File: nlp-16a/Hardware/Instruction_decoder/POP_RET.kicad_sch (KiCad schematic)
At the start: 12 parts

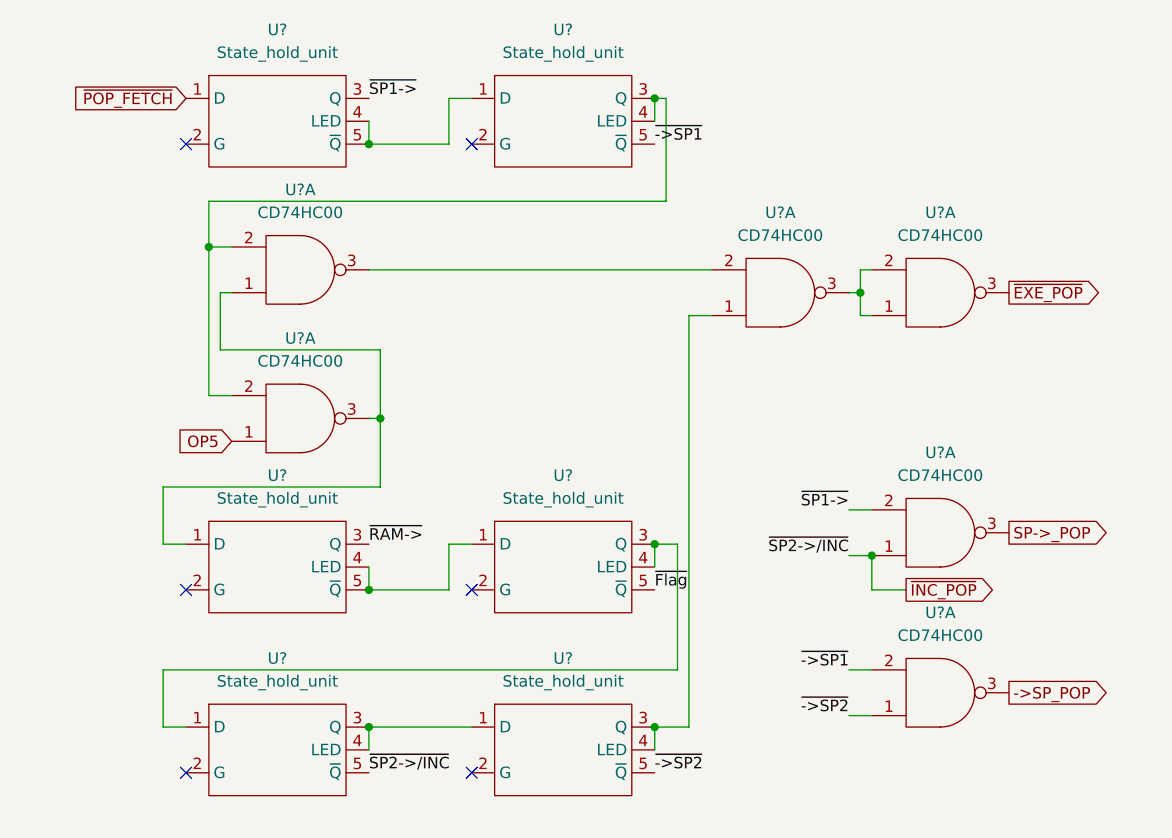
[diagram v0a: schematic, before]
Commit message: 命令デコーダ 不具合修正
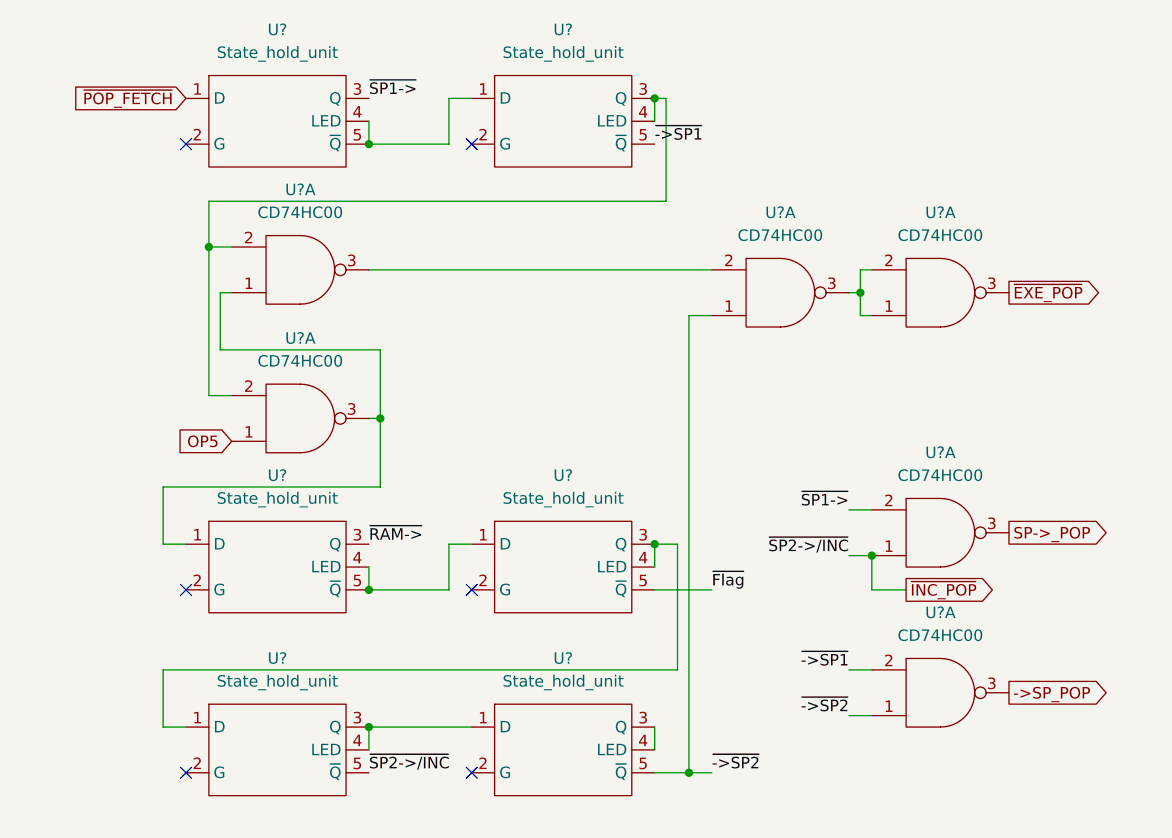
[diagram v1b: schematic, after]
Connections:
- net ~{->SP2}: now also U?.1
- net at U?.3 (Q), U?.4 (LED): no longer U?.1
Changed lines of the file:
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@@
   (junction (at 110.49 101.6) (diameter 0) (color 0 0 0 0)
   )
-  (junction (at 142.24 101.6) (diameter 0) (color 0 0 0 0)
-  )
   (junction (at 165.1 53.34) (diameter 0) (color 0 0 0 0)
   )
@@
   )
   (junction (at 142.24 81.28) (diameter 0) (color 0 0 0 0)
+  )
+  (junction (at 146.05 106.68) (diameter 0) (color 0 0 0 0)
   )
   (junction (at 110.49 36.83) (diameter 0) (color 0 0 0 0)
@@
     (stroke (width 0) (type default) (color 0 0 0 0))
   )
+  (wire (pts (xy 148.59 86.36) (xy 142.24 86.36))
+    (stroke (width 0) (type default) (color 0 0 0 0))
+  )
   (wire (pts (xy 111.76 67.31) (xy 111.76 74.93))
     (stroke (width 0) (type default) (color 0 0 0 0))
@@
     (stroke (width 0) (type default) (color 0 0 0 0))
   )
+  (wire (pts (xy 146.05 106.68) (xy 142.24 106.68))
+    (stroke (width 0) (type default) (color 0 0 0 0))
+  )
   (wire (pts (xy 142.24 31.75) (xy 143.51 31.75))
     (stroke (width 0) (type default) (color 0 0 0 0))
@@
     (stroke (width 0) (type default) (color 0 0 0 0))
   )
-  (wire (pts (xy 142.24 101.6) (xy 146.05 101.6))
-    (stroke (width 0) (type default) (color 0 0 0 0))
-  )
   (wire (pts (xy 142.24 31.75) (xy 142.24 34.29))
     (stroke (width 0) (type default) (color 0 0 0 0))
@@
     (stroke (width 0) (type default) (color 0 0 0 0))
   )
-  (wire (pts (xy 146.05 101.6) (xy 146.05 55.88))
+  (wire (pts (xy 146.05 55.88) (xy 146.05 106.68))
     (stroke (width 0) (type default) (color 0 0 0 0))
   )
@@
     (stroke (width 0) (type default) (color 0 0 0 0))
   )
+  (wire (pts (xy 148.59 106.68) (xy 146.05 106.68))
+    (stroke (width 0) (type default) (color 0 0 0 0))
+  )
   (wire (pts (xy 144.78 81.28) (xy 144.78 95.25))
     (stroke (width 0) (type default) (color 0 0 0 0))
@@
     (effects (font (size 1.27 1.27)) (justify left bottom))
   )
-  (label "~{Flag}" (at 142.24 86.36 0)
-    (effects (font (size 1.27 1.27)) (justify left bottom))
-  )
-  (label "~{->SP2}" (at 142.24 106.68 0)
-    (effects (font (size 1.27 1.27)) (justify left bottom))
-  )
+  (label "~{Flag}" (at 148.59 86.36 0)
+    (effects (font (size 1.27 1.27)) (justify left bottom))
+  )
+  (label "~{->SP2}" (at 148.59 106.68 0)
+    (effects (font (size 1.27 1.27)) (justify left bottom))
+  )

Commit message: 命令デコーダ ロジック部の設計だいたい完了git statusgit statusやったぜ
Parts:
- removed U? (x2): CD74HC00, Package_DIP:DIP-14_W7.62mm, symbol CD74HCXX:CD74HC00
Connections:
- net ~{->SP1} renamed ~{->SP_SET}
- net ~{->SP2} renamed ~{->SP_INC_RET}
- net ~{Flag} renamed ~{->Flag_Return}
- net ~{INC_POP} renamed ~{SP_INC_RET->}
- net ~{RAM->} renamed ~{Flag_Return->}
- net ~{SP1->} renamed ~{SP_SET->}
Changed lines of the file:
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@@
   (junction (at 165.1 53.34) (diameter 0) (color 0 0 0 0)
-  )
-  (junction (at 166.37 82.55) (diameter 0) (color 0 0 0 0)
   )
   (junction (at 142.24 31.75) (diameter 0) (color 0 0 0 0)
@@
   (no_connect (at 121.92 86.36))
   (no_connect (at 90.17 106.68))
-  (wire (pts (xy 166.37 82.55) (xy 166.37 86.36))
+  (wire (pts (xy 142.24 36.83) (xy 148.59 36.83))
     (stroke (width 0) (type default) (color 0 0 0 0))
   )
@@
     (stroke (width 0) (type default) (color 0 0 0 0))
   )
+  (wire (pts (xy 113.03 73.66) (xy 148.59 73.66))
+    (stroke (width 0) (type default) (color 0 0 0 0))
+  )
   (wire (pts (xy 146.05 55.88) (xy 148.59 55.88))
     (stroke (width 0) (type default) (color 0 0 0 0))
@@
     (stroke (width 0) (type default) (color 0 0 0 0))
   )
+  (wire (pts (xy 111.76 31.75) (xy 111.76 26.67))
+    (stroke (width 0) (type default) (color 0 0 0 0))
+  )
   (wire (pts (xy 142.24 81.28) (xy 144.78 81.28))
     (stroke (width 0) (type default) (color 0 0 0 0))
@@
     (stroke (width 0) (type default) (color 0 0 0 0))
   )
+  (wire (pts (xy 110.49 31.75) (xy 111.76 31.75))
+    (stroke (width 0) (type default) (color 0 0 0 0))
+  )
   (wire (pts (xy 143.51 43.18) (xy 92.71 43.18))
     (stroke (width 0) (type default) (color 0 0 0 0))
@@
     (stroke (width 0) (type default) (color 0 0 0 0))
   )
+  (wire (pts (xy 111.76 106.68) (xy 111.76 110.49))
+    (stroke (width 0) (type default) (color 0 0 0 0))
+  )
   (wire (pts (xy 142.24 101.6) (xy 142.24 104.14))
     (stroke (width 0) (type default) (color 0 0 0 0))
@@
     (stroke (width 0) (type default) (color 0 0 0 0))
   )
-  (wire (pts (xy 163.83 82.55) (xy 166.37 82.55))
-    (stroke (width 0) (type default) (color 0 0 0 0))
-  )
-  (wire (pts (xy 170.18 86.36) (xy 166.37 86.36))
+  (wire (pts (xy 113.03 81.28) (xy 113.03 73.66))
+    (stroke (width 0) (type default) (color 0 0 0 0))
+  )
+  (wire (pts (xy 111.76 110.49) (xy 148.59 110.49))
     (stroke (width 0) (type default) (color 0 0 0 0))
   )
@@
     (stroke (width 0) (type default) (color 0 0 0 0))
   )
-  (wire (pts (xy 163.83 77.47) (xy 166.37 77.47))
+  (wire (pts (xy 110.49 106.68) (xy 111.76 106.68))
+    (stroke (width 0) (type default) (color 0 0 0 0))
+  )
+  (wire (pts (xy 110.49 81.28) (xy 113.03 81.28))
     (stroke (width 0) (type default) (color 0 0 0 0))
   )
@@
     (stroke (width 0) (type default) (color 0 0 0 0))
   )
+  (wire (pts (xy 111.76 26.67) (xy 148.59 26.67))
+    (stroke (width 0) (type default) (color 0 0 0 0))
+  )
   (wire (pts (xy 90.17 101.6) (xy 87.63 101.6))
     (stroke (width 0) (type default) (color 0 0 0 0))
@@
     (stroke (width 0) (type default) (color 0 0 0 0))
   )
-  (wire (pts (xy 163.83 95.25) (xy 166.37 95.25))
-    (stroke (width 0) (type default) (color 0 0 0 0))
-  )
   (wire (pts (xy 143.51 31.75) (xy 143.51 43.18))
     (stroke (width 0) (type default) (color 0 0 0 0))
@@
     (stroke (width 0) (type default) (color 0 0 0 0))
   )
-  (wire (pts (xy 163.83 100.33) (xy 166.37 100.33))
-    (stroke (width 0) (type default) (color 0 0 0 0))
-  )
   (wire (pts (xy 163.83 53.34) (xy 165.1 53.34))
     (stroke (width 0) (type default) (color 0 0 0 0))
@@
     (stroke (width 0) (type default) (color 0 0 0 0))
   )
-  (label "~{SP1->}" (at 163.83 77.47 180)
-    (effects (font (size 1.27 1.27)) (justify right bottom))
-  )
-  (label "~{->SP1}" (at 163.83 95.25 180)
-    (effects (font (size 1.27 1.27)) (justify right bottom))
-  )
-  (label "~{SP2->{slash}INC}" (at 110.49 106.68 0)
-    (effects (font (size 1.27 1.27)) (justify left bottom))
-  )
-  (label "~{->SP2}" (at 163.83 100.33 180)
-    (effects (font (size 1.27 1.27)) (justify right bottom))
-  )
-  (label "~{SP2->{slash}INC}" (at 163.83 82.55 180)
-    (effects (font (size 1.27 1.27)) (justify right bottom))
-  )
-  (label "~{SP1->}" (at 110.49 31.75 0)
-    (effects (font (size 1.27 1.27)) (justify left bottom))
-  )
-  (label "~{RAM->}" (at 110.49 81.28 0)
-    (effects (font (size 1.27 1.27)) (justify left bottom))
-  )
-  (label "~{->SP1}" (at 142.24 36.83 0)
-    (effects (font (size 1.27 1.27)) (justify left bottom))
-  )
-  (label "~{Flag}" (at 148.59 86.36 0)
-    (effects (font (size 1.27 1.27)) (justify left bottom))
-  )
-  (label "~{->SP2}" (at 148.59 106.68 0)
-    (effects (font (size 1.27 1.27)) (justify left bottom))
-  )
   (global_label "~{EXE_POP}" (shape output) (at 181.61 53.34 0) (fields_autoplaced)
     (effects (font (size 1.27 1.27)) (justify left))
     (property "Intersheet References" "${INTERSHEET_REFS}" (id 0) (at 192.3688 53.2606 0)
+      (effects (font (size 1.27 1.27)) (justify left) hide)
+    )
+  )
+  (global_label "~{SP_INC_RET->}" (shape output) (at 148.59 110.49 0) (fields_autoplaced)
+    (effects (font (size 1.27 1.27)) (justify left))
+    (property "Intersheet References" "${INTERSHEET_REFS}" (id 0) (at 165.1545 110.4106 0)
       (effects (font (size 1.27 1.27)) (justify left) hide)
     )
@@
     )
   )
-  (global_label "SP->_POP" (shape output) (at 181.61 80.01 0) (fields_autoplaced)
-    (effects (font (size 1.27 1.27)) (justify left))
-    (property "Intersheet References" "${INTERSHEET_REFS}" (id 0) (at 194.4855 79.9306 0)
+  (global_label "~{->SP_INC_RET}" (shape output) (at 148.59 106.68 0) (fields_autoplaced)
+    (effects (font (size 1.27 1.27)) (justify left))
+    (property "Intersheet References" "${INTERSHEET_REFS}" (id 0) (at 165.1545 106.6006 0)
+      (effects (font (size 1.27 1.27)) (justify left) hide)
+    )
+  )
+  (global_label "~{SP_SET->}" (shape output) (at 148.59 26.67 0) (fields_autoplaced)
+    (effects (font (size 1.27 1.27)) (justify left))
+    (property "Intersheet References" "${INTERSHEET_REFS}" (id 0) (at 160.9212 26.5906 0)
+      (effects (font (size 1.27 1.27)) (justify left) hide)
+    )
+  )
+  (global_label "~{->SP_SET}" (shape output) (at 148.59 36.83 0) (fields_autoplaced)
+    (effects (font (size 1.27 1.27)) (justify left))
+    (property "Intersheet References" "${INTERSHEET_REFS}" (id 0) (at 160.9212 36.7506 0)
       (effects (font (size 1.27 1.27)) (justify left) hide)
     )
@@
     )
   )
-  (global_label "->SP_POP" (shape output) (at 181.61 97.79 0) (fields_autoplaced)
-    (effects (font (size 1.27 1.27)) (justify left))
-    (property "Intersheet References" "${INTERSHEET_REFS}" (id 0) (at 194.4855 97.7106 0)
-      (effects (font (size 1.27 1.27)) (justify left) hide)
-    )
-  )
-  (global_label "~{INC_POP}" (shape output) (at 170.18 86.36 0) (fields_autoplaced)
-    (effects (font (size 1.27 1.27)) (justify left))
-    (property "Intersheet References" "${INTERSHEET_REFS}" (id 0) (at 180.6364 86.2806 0)
+  (global_label "~{Flag_Return->}" (shape output) (at 148.59 73.66 0) (fields_autoplaced)
+    (effects (font (size 1.27 1.27)) (justify left))
+    (property "Intersheet References" "${INTERSHEET_REFS}" (id 0) (at 165.336 73.5806 0)
+      (effects (font (size 1.27 1.27)) (justify left) hide)
+    )
+  )
+  (global_label "~{->Flag_Return}" (shape output) (at 148.59 86.36 0) (fields_autoplaced)
+    (effects (font (size 1.27 1.27)) (justify left))
+    (property "Intersheet References" "${INTERSHEET_REFS}" (id 0) (at 165.336 86.2806 0)
       (effects (font (size 1.27 1.27)) (justify left) hide)
     )
@@
     (pin "14")
     (pin "7")
-    (pin "1")
-    (pin "2")
-    (pin "3")
-    (pin "4")
-    (pin "5")
-    (pin "6")
-    (pin "10")
-    (pin "8")
-    (pin "9")
-    (pin "11")
-    (pin "12")
-    (pin "13")
-  )
-  (symbol (lib_id "CD74HCXX:CD74HC00") (at 173.99 80.01 0) (mirror x) (unit 1)
-    (in_bom yes) (on_board yes)
-    (property "Reference" "U?" (id 0) (at 173.99 71.12 0))
-    (property "Value" "CD74HC00" (id 1) (at 173.99 73.66 0))
-    (property "Footprint" "Package_DIP:DIP-14_W7.62mm" (id 2) (at 173.99 86.36 0)
-      (effects (font (size 1.27 1.27)) hide)
-    )
-    (property "Datasheet" "" (id 3) (at 168.91 80.01 0))
-    (pin "14")
-    (pin "7")
-    (pin "1")
-    (pin "2")
-    (pin "3")
-    (pin "4")
-    (pin "5")
-    (pin "6")
-    (pin "10")
-    (pin "8")
-    (pin "9")
-    (pin "11")
-    (pin "12")
-    (pin "13")
-  )
-  (symbol (lib_id "CD74HCXX:CD74HC00") (at 173.99 97.79 0) (mirror x) (unit 1)
-    (in_bom yes) (on_board yes)
-    (property "Reference" "U?" (id 0) (at 173.99 88.9 0))
-    (property "Value" "CD74HC00" (id 1) (at 173.99 91.44 0))
-    (property "Footprint" "Package_DIP:DIP-14_W7.62mm" (id 2) (at 173.99 104.14 0)
-      (effects (font (size 1.27 1.27)) hide)
-    )
-    (property "Datasheet" "" (id 3) (at 168.91 97.79 0))
-    (pin "14")
-    (pin "7")

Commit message: アノテーションまで完了．基板設計に入る
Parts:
- gave numbers to parts that had none: 7
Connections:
- net OP5: now also U61.12; no longer U61.1
- net ~{EXE_POP}: now also U61.6; no longer U61.3
- net at U30.3 (Q), U30.4 (LED): now also U61.10, U61.13; no longer U61.2, U61.2
- net at U61.2: now also U61.8; no longer U61.3
- new net: U61.3, U61.4, U61.5
- new net: U31.1 (D), U61.11, U61.9
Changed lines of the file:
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@@
   (symbol (lib_id "State_hold_unit:State_hold_unit") (at 132.08 27.94 0) (unit 1)
     (in_bom yes) (on_board yes) (fields_autoplaced)
-    (property "Reference" "U?" (id 0) (at 132.08 24.13 0))
+    (property "Reference" "U30" (id 0) (at 132.08 24.13 0))
     (property "Value" "State_hold_unit" (id 1) (at 132.08 26.67 0))
     (property "Footprint" "" (id 2) (at 132.08 27.94 0)
@@
     (pin "5")
   )
-  (symbol (lib_id "CD74HCXX:CD74HC00") (at 173.99 53.34 0) (mirror x) (unit 1)
+  (symbol (lib_id "CD74HCXX:CD74HC00") (at 173.99 53.34 0) (mirror x) (unit 2)
     (in_bom yes) (on_board yes)
-    (property "Reference" "U?" (id 0) (at 173.99 44.45 0))
+    (property "Reference" "U61" (id 0) (at 173.99 44.45 0))
     (property "Value" "CD74HC00" (id 1) (at 173.99 46.99 0))
     (property "Footprint" "Package_DIP:DIP-14_W7.62mm" (id 2) (at 173.99 59.69 0)
@@
   (symbol (lib_id "State_hold_unit:State_hold_unit") (at 100.33 27.94 0) (unit 1)
     (in_bom yes) (on_board yes) (fields_autoplaced)
-    (property "Reference" "U?" (id 0) (at 100.33 24.13 0))
+    (property "Reference" "U29" (id 0) (at 100.33 24.13 0))
     (property "Value" "State_hold_unit" (id 1) (at 100.33 26.67 0))
     (property "Footprint" "" (id 2) (at 100.33 27.94 0)
@@
   (symbol (lib_id "State_hold_unit:State_hold_unit") (at 132.08 77.47 0) (unit 1)
     (in_bom yes) (on_board yes) (fields_autoplaced)
-    (property "Reference" "U?" (id 0) (at 132.08 73.66 0))
+    (property "Reference" "U32" (id 0) (at 132.08 73.66 0))
     (property "Value" "State_hold_unit" (id 1) (at 132.08 76.2 0))
     (property "Footprint" "" (id 2) (at 132.08 77.47 0)
@@
   (symbol (lib_id "State_hold_unit:State_hold_unit") (at 100.33 97.79 0) (unit 1)
     (in_bom yes) (on_board yes) (fields_autoplaced)
-    (property "Reference" "U?" (id 0) (at 100.33 93.98 0))
+    (property "Reference" "U33" (id 0) (at 100.33 93.98 0))
     (property "Value" "State_hold_unit" (id 1) (at 100.33 96.52 0))
     (property "Footprint" "" (id 2) (at 100.33 97.79 0)
@@
     (pin "5")
   )
-  (symbol (lib_id "CD74HCXX:CD74HC00") (at 102.87 50.8 0) (mirror x) (unit 1)
+  (symbol (lib_id "CD74HCXX:CD74HC00") (at 102.87 50.8 0) (mirror x) (unit 3)
     (in_bom yes) (on_board yes)
-    (property "Reference" "U?" (id 0) (at 102.87 41.91 0))
+    (property "Reference" "U61" (id 0) (at 102.87 41.91 0))
     (property "Value" "CD74HC00" (id 1) (at 102.87 44.45 0))
     (property "Footprint" "Package_DIP:DIP-14_W7.62mm" (id 2) (at 102.87 57.15 0)
@@
     (pin "13")
   )
-  (symbol (lib_id "CD74HCXX:CD74HC00") (at 102.87 67.31 0) (mirror x) (unit 1)
+  (symbol (lib_id "CD74HCXX:CD74HC00") (at 102.87 67.31 0) (mirror x) (unit 4)
     (in_bom yes) (on_board yes)
-    (property "Reference" "U?" (id 0) (at 102.87 58.42 0))
+    (property "Reference" "U61" (id 0) (at 102.87 58.42 0))
     (property "Value" "CD74HC00" (id 1) (at 102.87 60.96 0))
     (property "Footprint" "Package_DIP:DIP-14_W7.62mm" (id 2) (at 102.87 73.66 0)
@@
   (symbol (lib_id "State_hold_unit:State_hold_unit") (at 100.33 77.47 0) (unit 1)
     (in_bom yes) (on_board yes) (fields_autoplaced)
-    (property "Reference" "U?" (id 0) (at 100.33 73.66 0))
+    (property "Reference" "U31" (id 0) (at 100.33 73.66 0))
     (property "Value" "State_hold_unit" (id 1) (at 100.33 76.2 0))
     (property "Footprint" "" (id 2) (at 100.33 77.47 0)
@@
   (symbol (lib_id "CD74HCXX:CD74HC00") (at 156.21 53.34 0) (mirror x) (unit 1)
     (in_bom yes) (on_board yes)
-    (property "Reference" "U?" (id 0) (at 156.21 44.45 0))
+    (property "Reference" "U61" (id 0) (at 156.21 44.45 0))
     (property "Value" "CD74HC00" (id 1) (at 156.21 46.99 0))
     (property "Footprint" "Package_DIP:DIP-14_W7.62mm" (id 2) (at 156.21 59.69 0)
@@
   (symbol (lib_id "State_hold_unit:State_hold_unit") (at 132.08 97.79 0) (unit 1)
     (in_bom yes) (on_board yes) (fields_autoplaced)
-    (property "Reference" "U?" (id 0) (at 132.08 93.98 0))
+    (property "Reference" "U34" (id 0) (at 132.08 93.98 0))
     (property "Value" "State_hold_unit" (id 1) (at 132.08 96.52 0))
     (property "Footprint" "" (id 2) (at 132.08 97.79 0)
